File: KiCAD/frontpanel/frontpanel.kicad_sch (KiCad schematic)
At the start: 29 parts, among them J1 8P8C_Shielded, J2 Conn_01x03_Pin, Q1 2N7000, Q2 2N7000, Q3 2N7000, U1 Adafruit_PCF8575_Breakout, U2 MCP4725

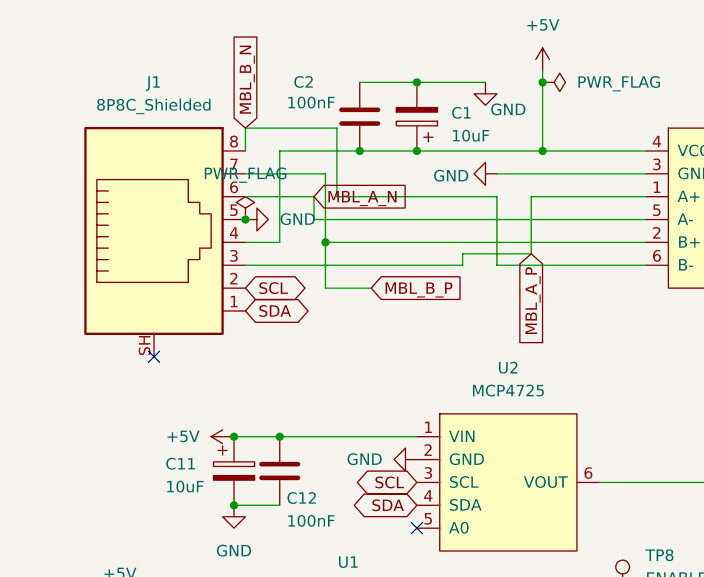
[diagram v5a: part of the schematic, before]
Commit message: schematic: revB encoder interrupt rerouted through CAT6 umbilical
- interface.kicad_sch: ENC_INT global label (input) replaces the old
  direct wire+GND stub; encoder interrupt now travels over the RJ45
  cable with the shield as signal return
- frontpanel.kicad_sch: 4-pin header J (Conn_01x04) added for up to
  3 encoder connections + one test-point pin; ENC_INT_IN label wired in
- arduino.kicad_sch: removed orphaned Conn_Coaxial symbol cache
- vfo.kicad_sch: minor layout/annotation updates

Co-Authored-By: Claude Sonnet 4.6 (1M context) <noreply@anthropic.com>
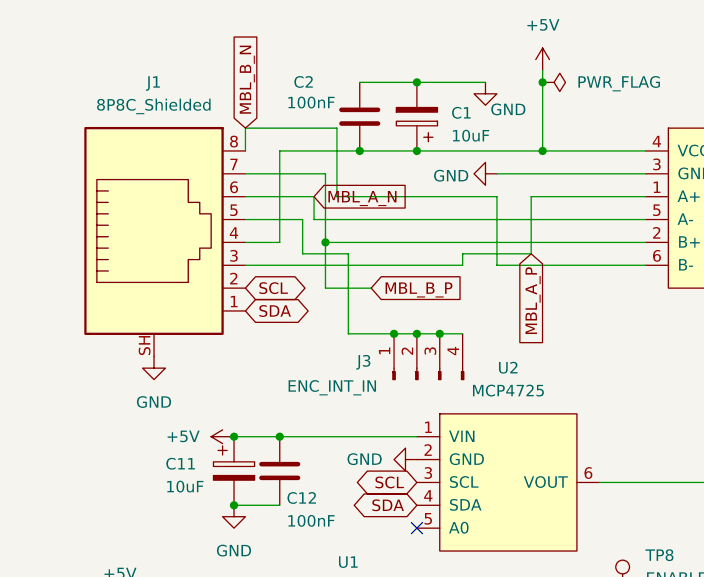
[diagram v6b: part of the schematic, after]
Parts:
- added J3: ENC_INT_IN, symbol Connector:Conn_01x04_Pin
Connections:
- net GND: now also J1.SH; no longer J1.5
- new net: J1.5, J3.1 (Pin_1), J3.2 (Pin_2), J3.3 (Pin_3), J3.4 (Pin_4)
- no-connect marks 5 -> 4
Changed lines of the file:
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@@
 	)
 	(junction
-		(at 43.18 87.63)
+		(at 59.69 100.33)
+		(diameter 0)
+		(color 0 0 0 0)
+	)
+	(junction
+		(at 64.77 100.33)
+		(diameter 0)
+		(color 0 0 0 0)
+	)
+	(junction
+		(at 62.23 100.33)
 		(diameter 0)
 		(color 0 0 0 0)
@@
 	)
 	(no_connect
-		(at 33.02 102.87)
-	)
-	(no_connect
 		(at 63.5 132.08)
 	)
@@
 	(wire
 		(pts
+			(xy 54.61 100.33) (xy 59.69 100.33)
+		)
+		(stroke
+			(width 0)
+			(type default)
+		)
+	)
+	(wire
+		(pts
 			(xy 43.18 85.09) (xy 50.8 85.09)
 		)
@@
 	(wire
 		(pts
+			(xy 43.18 87.63) (xy 49.53 87.63)
+		)
+		(stroke
+			(width 0)
+			(type default)
+		)
+	)
+	(wire
+		(pts
+			(xy 49.53 87.63) (xy 49.53 91.44)
+		)
+		(stroke
+			(width 0)
+			(type default)
+		)
+	)
+	(wire
+		(pts
 			(xy 67.31 92.71) (xy 43.18 92.71)
 		)
@@
 	(wire
 		(pts
+			(xy 64.77 100.33) (xy 67.31 100.33)
+		)
+		(stroke
+			(width 0)
+			(type default)
+		)
+	)
+	(wire
+		(pts
 			(xy 35.56 160.02) (xy 45.72 160.02)
 		)
@@
 	(wire
 		(pts
+			(xy 54.61 91.44) (xy 54.61 100.33)
+		)
+		(stroke
+			(width 0)
+			(type default)
+		)
+	)
+	(wire
+		(pts
 			(xy 124.46 119.38) (xy 124.46 111.76)
 		)
@@
 	(wire
 		(pts
+			(xy 49.53 91.44) (xy 54.61 91.44)
+		)
+		(stroke
+			(width 0)
+			(type default)
+		)
+	)
+	(wire
+		(pts
 			(xy 35.56 144.78) (xy 45.72 144.78)
 		)
@@
 	(wire
 		(pts
+			(xy 62.23 100.33) (xy 64.77 100.33)
+		)
+		(stroke
+			(width 0)
+			(type default)
+		)
+	)
+	(wire
+		(pts
 			(xy 123.19 132.08) (xy 130.81 132.08)
 		)
@@
 	(wire
 		(pts
+			(xy 59.69 100.33) (xy 62.23 100.33)
+		)
+		(stroke
+			(width 0)
+			(type default)
+		)
+	)
+	(wire
+		(pts
 			(xy 52.07 90.17) (xy 52.07 95.25)
 		)
@@
 	)
 	(symbol
-		(lib_id "power:PWR_FLAG")
-		(at 43.18 87.63 0)
+		(lib_id "Connector:Conn_01x04_Pin")
+		(at 62.23 105.41 90)
 		(unit 1)
 		(body_style 1)
@@
 		(in_pos_files yes)
 		(dnp no)
-		(fields_autoplaced yes)
-		(property "Reference" "#FLG02"
-			(at 43.18 85.725 0)
-			(hide yes)
+		(property "Reference" "J3"
+			(at 56.388 103.378 90)
 			(show_name no)
 			(do_not_autoplace no)
@@
 			)
 		)
-		(property "Value" "PWR_FLAG"
-			(at 43.18 82.55 0)
+		(property "Value" "ENC_INT_IN"
+			(at 52.832 106.172 90)
 			(show_name no)
 			(do_not_autoplace no)
@@
 		)
 		(property "Footprint" ""
-			(at 43.18 87.63 0)
+			(at 62.23 105.41 0)
 			(hide yes)
 			(show_name no)
@@
 		)
 		(property "Datasheet" ""
-			(at 43.18 87.63 0)
+			(at 62.23 105.41 0)
 			(hide yes)
 			(show_name no)
@@
 			)
 		)
-		(property "Description" "Special symbol for telling ERC where power comes from"
-			(at 43.18 87.63 0)
+		(property "Description" "Generic connector, single row, 01x04, script generated"
+			(at 62.23 105.41 0)
 			(hide yes)
 			(show_name no)
@@
 			)
 		)
+		(pin "3"
+		)
 		(pin "1"
 		)
+		(pin "2"
+		)
+		(pin "4"
+		)
 		(instances
 			(project "frontpanel"
 				(path "/ee8ebf10-f58c-4b1e-9881-a5464c055387"
-					(reference "#FLG02")
+					(reference "J3")
 					(unit 1)
 				)
@@
 	)
 	(symbol
-		(lib_id "power:GND")
-		(at 43.18 87.63 90)
-		(unit 1)
-		(body_style 1)
-		(exclude_from_sim no)
-		(in_bom yes)
-		(on_board yes)
-		(in_pos_files yes)
-		(dnp no)
-		(fields_autoplaced yes)
-		(property "Reference" "#PWR03"
-			(at 49.53 87.63 0)
-			(hide yes)
-			(show_name no)
-			(do_not_autoplace no)
-			(effects
-				(font
-					(size 1.27 1.27)
-				)
-			)
-		)
-		(property "Value" "GND"
-			(at 46.99 87.6299 90)
-			(show_name no)
-			(do_not_autoplace no)
-			(effects
-				(font
-					(size 1.27 1.27)
-				)
-				(justify right)
-			)
-		)
-		(property "Footprint" ""
-			(at 43.18 87.63 0)
-			(hide yes)
-			(show_name no)
-			(do_not_autoplace no)
-			(effects
-				(font
-					(size 1.27 1.27)
-				)
-			)
-		)
-		(property "Datasheet" ""
-			(at 43.18 87.63 0)
-			(hide yes)
-			(show_name no)
-			(do_not_autoplace no)
-			(effects
-				(font
-					(size 1.27 1.27)
-				)
-			)
-		)
-		(property "Description" "Power symbol creates a global label with name \"GND\" , ground"
-			(at 43.18 87.63 0)
-			(hide yes)
-			(show_name no)
-			(do_not_autoplace no)
-			(effects
-				(font
-					(size 1.27 1.27)
-				)
-			)
-		)
-		(pin "1"
-		)
-		(instances
-			(project "frontpanel"
-				(path "/ee8ebf10-f58c-4b1e-9881-a5464c055387"
-					(reference "#PWR03")
-					(unit 1)
-				)
-			)
-		)
-	)
-	(symbol
 		(lib_id "xmitter:MCP4725")
 		(at 72.39 116.84 0)
@@
 					(unit 1)
 				)
+			)
+		)
+	)
+	(symbol
+		(lib_id "power:GND")
+		(at 33.02 102.87 0)
+		(unit 1)
+		(body_style 1)
+		(exclude_from_sim no)
+		(in_bom yes)
+		(on_board yes)
+		(in_pos_files yes)
+		(dnp no)
+		(fields_autoplaced yes)
+		(property "Reference" "#PWR03"
+			(at 33.02 109.22 0)
+			(hide yes)
+			(show_name no)
+			(do_not_autoplace no)
+			(effects
+				(font
+					(size 1.27 1.27)
+				)
+			)
+		)
+		(property "Value" "GND"
+			(at 33.02 107.95 0)
+			(show_name no)
+			(do_not_autoplace no)
+			(effects
+				(font
+					(size 1.27 1.27)
+				)
+			)
+		)
+		(property "Footprint" ""
+			(at 33.02 102.87 0)
+			(hide yes)
+			(show_name no)
+			(do_not_autoplace no)
+			(effects
+				(font
+					(size 1.27 1.27)
+				)
+			)
+		)
+		(property "Datasheet" ""
+			(at 33.02 102.87 0)
+			(hide yes)
+			(show_name no)
+			(do_not_autoplace no)
+			(effects
+				(font
+					(size 1.27 1.27)
+				)
+			)
+		)
+		(property "Description" "Power symbol creates a global label with name \"GND\" , ground"
+			(at 33.02 102.87 0)
+			(hide yes)
+			(show_name no)
+			(do_not_autoplace no)
+			(effects
+				(font
+					(size 1.27 1.27)
+				)
+			)
+		)
+		(pin "1"
+		)
+		(instances
+			(project "frontpanel"
+				(path "/ee8ebf10-f58c-4b1e-9881-a5464c055387"
+					(reference "#PWR03")
+					(unit 1)
+				)

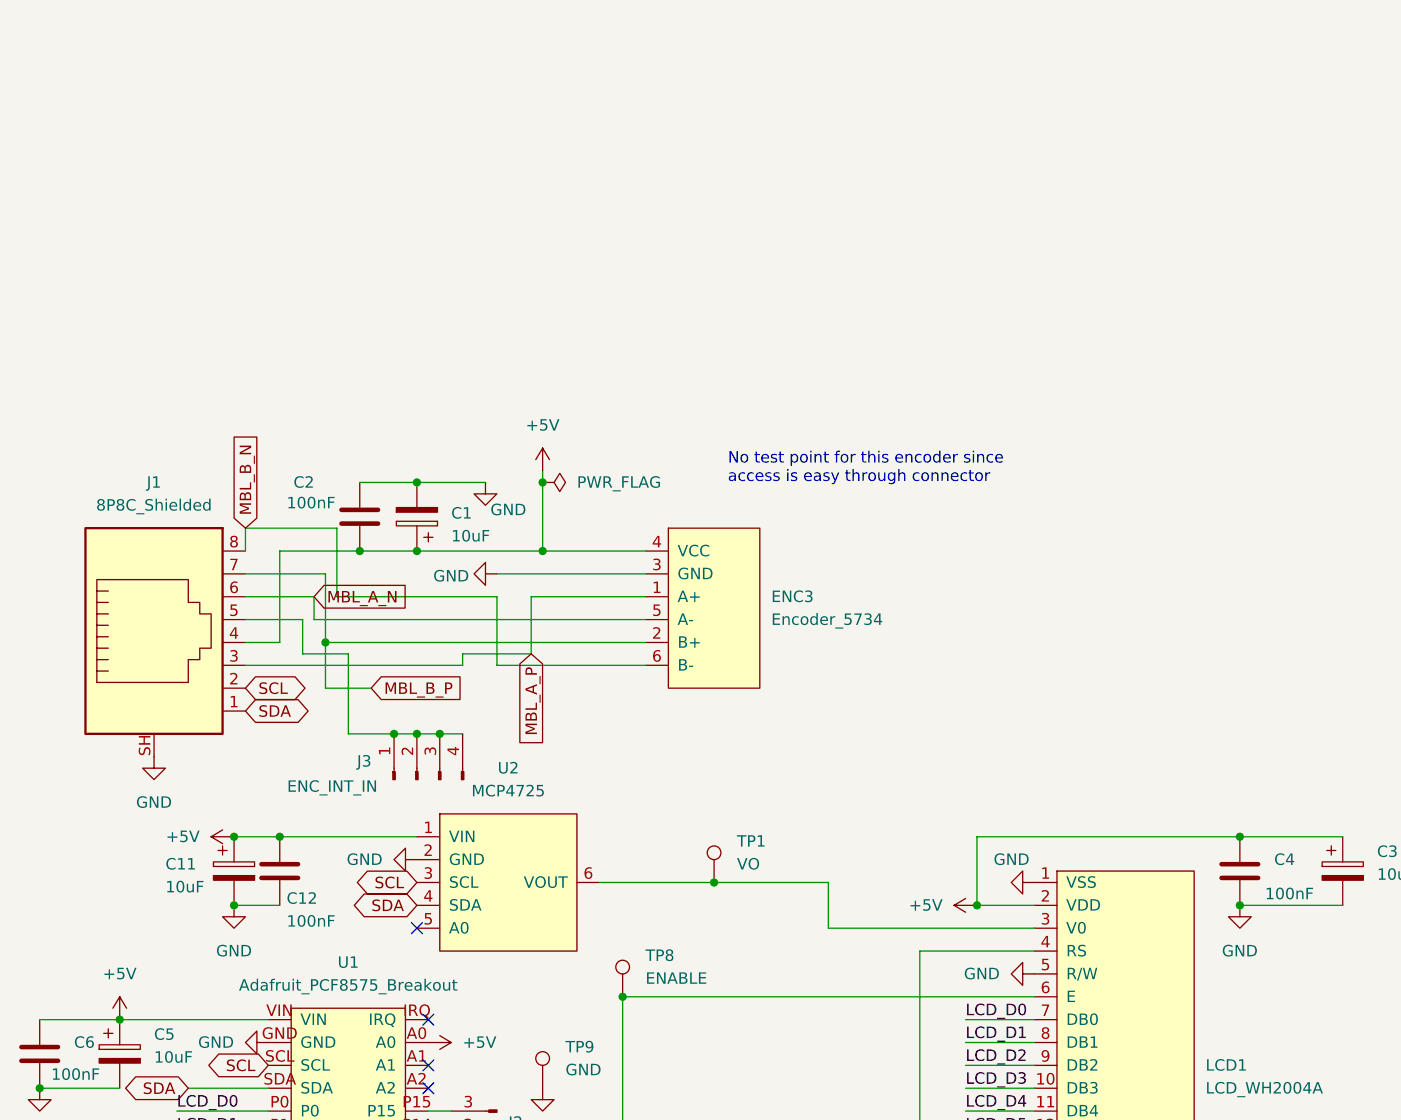
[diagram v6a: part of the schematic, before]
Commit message: KiCad revB: schematic review pass — I2C, ENC_INT, GND returns, GRID_BLOCK_CRASH clamp
Result of extended review pass against fresh netlists across all four
boards. All connectivity blockers resolved.

- Si5351 SDA/SCL wired via 0R jumpers (R8/R9) puts I2C on PCB traces
  for PCF8575 U17 and the RJ45 to the front panel. MCP4728 side has
  parallel 0R jumpers (R3/R4/R5) left DNP by default — STEMMA-QT is
  the intended path.
- ENC_INT chain unified end-to-end with staged names:
  ENC_INT_RAW (frontpanel encoder wire-OR) → ENC_INT_CLEAN (across
  CAT + analog pass-through) → ENC_INT_FINAL (post-protoshield
  conditioning). Frontpanel U4 (MCP1700-3.3 LDO) sources the +3.3V
  the pull-up R4 needs; pull-up moved to encoder side for sharper
  falling edges over the 2 m CAT run.
- Protoshield GRID_BLOCK_CRASH gets 1N4728A Zener clamp (D5),
  matching the I_CATHODE and MBL600 5V→3.3V clamp topology.
- Protoshield MBL600 conditioning rebuilt: 1K series + 100nF filter
  + 1N4728A clamp (was 10K/20K divider + 22pF that filtered nothing
  below RF).
- PADDLE_A/B and RESET_N removed from analog board — case-mounted
  switches wire directly to protoshield.
- Protoshield J1/J6 widened to 3-pin to include GND returns for the
  case-mounted paddle and reset switches.
- Bias board reference designators reorganized functionally
  (R_FA/R_FB feedback, R_GA/R_GB gain, R_PADA/R_PADB, R_GLA/R_GLB
  grid line, R_GATE, R_Z).
- New Documentation/control_board_functional_blocks.md captures
  KeyUp/Gate 2 keying, relay assignments (J6=T/R, J7=HV primary,
  J8=HV inrush), CD14538B heartbeat watchdog, TR_SENSE interlock,
  and J13 power-migration header.
- Fresh netlists exported for all four boards.

Co-Authored-By: Claude Opus 4.7 <noreply@anthropic.com>
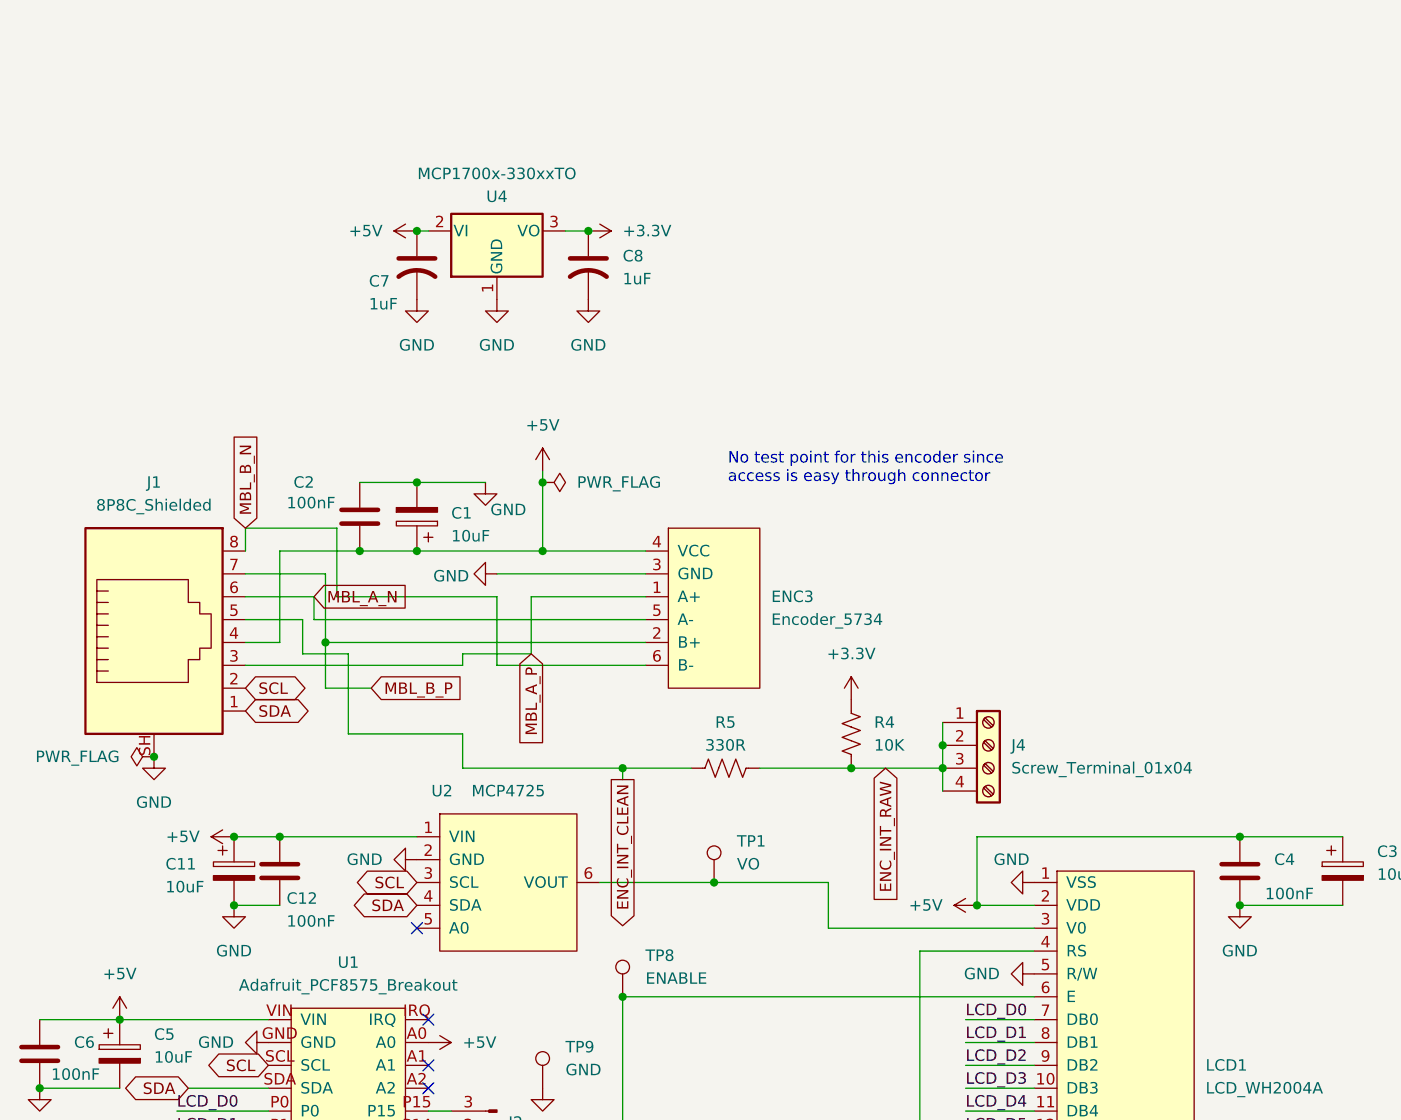
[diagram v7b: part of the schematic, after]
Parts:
- removed J3: ENC_INT_IN, symbol Connector:Conn_01x04_Pin
- added C7, C8: 1uF, symbol Device:C_US
- added J4: Screw_Terminal_01x04, symbol Connector:Screw_Terminal_01x04
- added R4: 10K, symbol Device:R_US
- added R5: 330R, symbol Device:R_US
- added U4: MCP1700x-330xxTO, Package_TO_SOT_THT:TO-92_Inline, symbol Regulator_Linear:MCP1700x-330xxTO
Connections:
- net +5V: now also C7.1, U4.2 (VI)
- net GND: now also C7.2, C8.2, U4.1 (GND)
- net ENC_INT_CLEAN: now reaches J1.5
- net ENC_INT_CLEAN: now also R5.1
- new net +3.3V: C8.1, R4.1, U4.3 (VO)
- new net ENC_INT_RAW: J4.1 (Pin_1), J4.2 (Pin_2), J4.3 (Pin_3), J4.4 (Pin_4), R4.2, R5.2

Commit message: KiCad revB: assign 87 empty footprints via re-runnable scripts
Filled empty Footprint fields on capacitors, resistors, and screw
terminals across all four boards. All three scripts are re-runnable
and only fill empty fields (never overwrite existing assignments).

Scripts:
- assign_cap_footprints.py: extended CAP_LIB_IDS to also cover
  Device:C_US, Device:C_Polarized_US, Device:C_Small (was only
  Device:C and Device:C_Polarized). VALUE_TO_FOOTPRINT map unchanged.
- assign_connector_footprints.py (new): matches
  Connector:Screw_Terminal_01xNN to Phoenix MKDS-1,5-N horizontal
  P5.00mm per pin count (same pattern the protoshield already used).
- assign_resistor_footprints.py (new): matches Device:R and
  Device:R_US to the project-standard Resistor_THT:R_Axial_DIN0207
  L6.3mm_D2.5mm_P10.16mm_Horizontal footprint. All 46 populated
  resistors on the project already used this footprint; the empty
  ones now match.

Assignment counts:
- Capacitors: 42 (5 arduino, 33 vfo_complete, 2 bias, 2 frontpanel)
- Screw terminals: 17 (10 arduino, 4 bias, 1 frontpanel, 2 protoshield)
- Resistors: 28 (5 arduino, 21 vfo_complete, 2 frontpanel)

Deferred (need part-specific decisions, tracked in review notes):
- Coax connectors (12 total across analog + bias) - awaiting Cinch
  142-0701-201 footprint verification in KiCad's Connector_Coaxial
  library, or a custom footprint in xmitter.pretty/
- One-off ICs: F1 Polyfuse, U3 MCP4728, U21 LT1054
- 6 unmapped cap values in vfo_complete: 2pF x3, 220nF, 4700uF, 100uF
- U2 Metro_ESP32S3 (protoshield): intentionally empty (on_board no,
  plug-in module, not placed on PCB)

Also add three component datasheets: 1N4736AT-D (1N4728A family
reference), LM393-D, OPA1641.

Co-Authored-By: Claude Opus 4.7 <noreply@anthropic.com>
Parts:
- C7, C8: footprint (none) -> Capacitor_THT:C_Rect_L7.2mm_W4.5mm_P5.00mm
- J4: footprint (none) -> TerminalBlock_Phoenix:TerminalBlock_Phoenix_MKDS-1,5-4_1x04_P5.00mm_Horizontal
- R4, R5: footprint (none) -> Resistor_THT:R_Axial_DIN0207_L6.3mm_D2.5mm_P10.16mm_Horizontal
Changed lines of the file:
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@@
 			)
 		)
-		(property "Footprint" ""
+		(property "Footprint" "Capacitor_THT:C_Rect_L7.2mm_W4.5mm_P5.00mm"
 			(at 62.23 48.26 0)
 			(hide yes)
@@
 			)
 		)
-		(property "Footprint" ""
+		(property "Footprint" "TerminalBlock_Phoenix:TerminalBlock_Phoenix_MKDS-1,5-4_1x04_P5.00mm_Horizontal"
 			(at 125.73 101.6 0)
 			(hide yes)
@@
 			)
 		)
-		(property "Footprint" ""
+		(property "Footprint" "Resistor_THT:R_Axial_DIN0207_L6.3mm_D2.5mm_P10.16mm_Horizontal"
 			(at 111.506 100.584 90)
 			(hide yes)
@@
 			)
 		)
-		(property "Footprint" ""
+		(property "Footprint" "Capacitor_THT:C_Rect_L7.2mm_W4.5mm_P5.00mm"
 			(at 81.28 48.26 0)
 			(hide yes)
@@
 			)
 		)
-		(property "Footprint" ""
+		(property "Footprint" "Resistor_THT:R_Axial_DIN0207_L6.3mm_D2.5mm_P10.16mm_Horizontal"
 			(at 96.774 103.124 90)
 			(hide yes)
